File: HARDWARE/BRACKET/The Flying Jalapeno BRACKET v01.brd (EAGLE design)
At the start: 5.1 x 15.2 mm, 0 parts

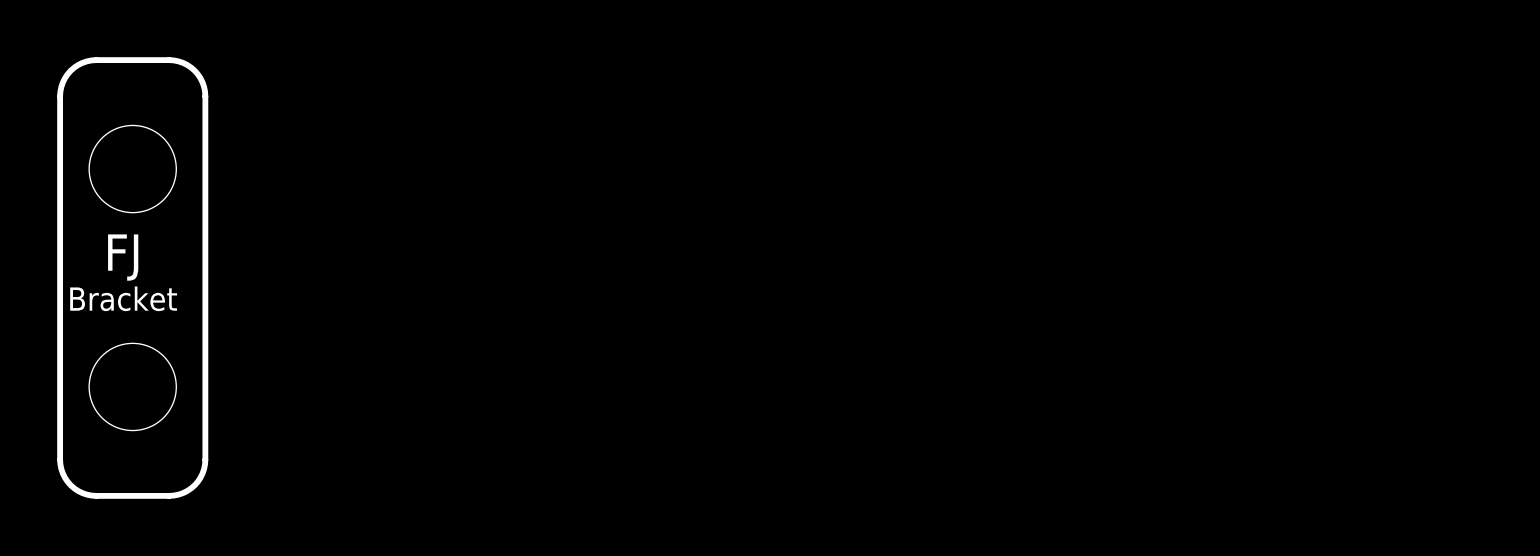
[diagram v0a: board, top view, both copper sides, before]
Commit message: Changed "FJ Bracket" text to tplace
also made the brd file have 8 copies, for quicker adding to QC panels
when we order a tone of these.
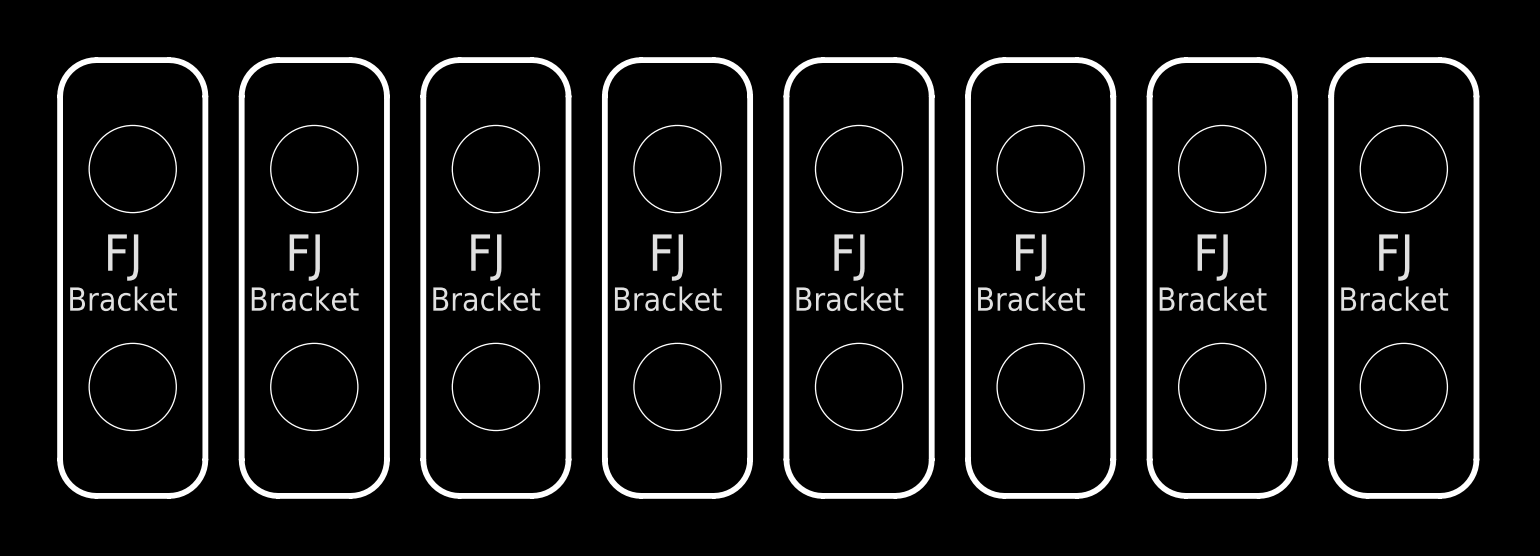
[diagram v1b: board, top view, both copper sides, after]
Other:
- board size 5.1 x 15.2 mm -> 49.5 x 15.2 mm
